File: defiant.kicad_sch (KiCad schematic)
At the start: 47 parts, among them J1 Conn_01x02_Pin, SW1 SW_Push, U1 Seeed Studio XIAO BLE

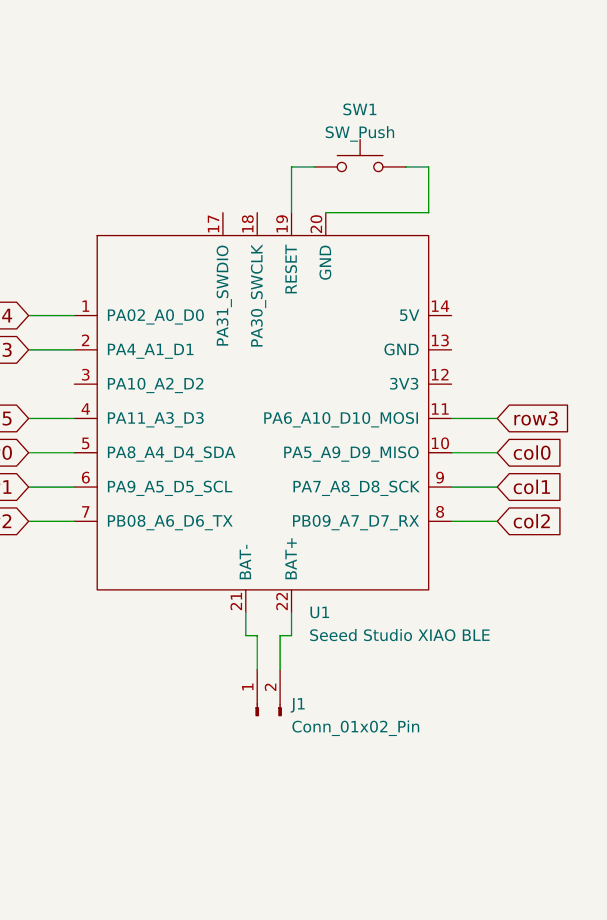
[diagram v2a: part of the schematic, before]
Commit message: Add power switch and reset button
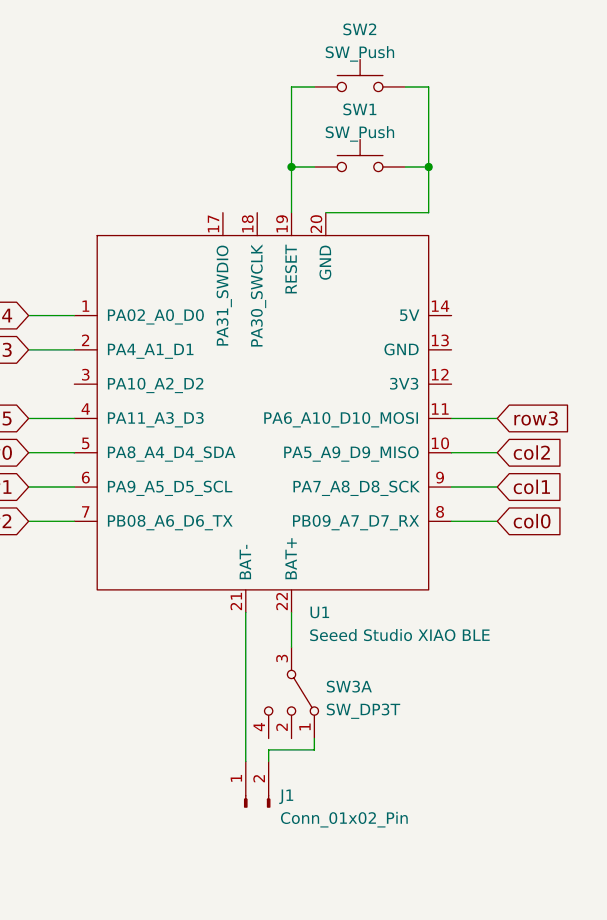
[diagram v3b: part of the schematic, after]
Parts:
- added SW2: SW_Push, Button_Switch_SMD:SW_SPST_TL3342, symbol Switch:SW_Push
- added SW3: SW_DP3T, Button_Switch_THT:SW_CuK_JS202011AQN_DPDT_Angled, symbol Switch:SW_DP3T
- SW1: footprint (none) -> Button_Switch_SMD:SW_SPST_TL3342
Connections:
- net col0: now also U1.8 (PB09_A7_D7_RX); no longer U1.10 (PA5_A9_D9_MISO)
- net col2: now also U1.10 (PA5_A9_D9_MISO); no longer U1.8 (PB09_A7_D7_RX)
- net at SW1.1, U1.19 (RESET): now also SW2.1
- net at SW1.2, U1.20 (GND): now also SW2.2
- net at U1.22 (BAT+): now also SW3.3; no longer J1.2 (Pin_2)
- new net: J1.2 (Pin_2), SW3.1
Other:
- moved on the sheet: J1
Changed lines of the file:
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@@
   (junction (at 97.79 69.85) (diameter 0) (color 0 0 0 0)
   )
+  (junction (at 243.84 27.94) (diameter 0) (color 0 0 0 0)
+  )
   (junction (at 36.83 45.72) (diameter 0) (color 0 0 0 0)
   )
@@
   (junction (at 74.93 69.85) (diameter 0) (color 0 0 0 0)
   )
+  (junction (at 228.6 27.94) (diameter 0) (color 0 0 0 0)
+  )
   (junction (at 143.51 69.85) (diameter 0) (color 0 0 0 0)
   )
@@
   (junction (at 36.83 77.47) (diameter 0) (color 0 0 0 0)
   )
-  (wire (pts (xy 224.79 83.82) (xy 224.79 80.01))
-    (stroke (width 0) (type default))
-  )
   (wire (pts (xy 105.41 62.23) (xy 105.41 77.47))
     (stroke (width 0) (type default))
@@
     (stroke (width 0) (type default))
   )
-  (wire (pts (xy 227.33 80.01) (xy 228.6 80.01))
-    (stroke (width 0) (type default))
-  )
   (wire (pts (xy 128.27 90.17) (xy 151.13 90.17))
     (stroke (width 0) (type default))
@@
     (stroke (width 0) (type default))
   )
-  (wire (pts (xy 228.6 80.01) (xy 228.6 77.47))
+  (wire (pts (xy 228.6 77.47) (xy 228.6 81.28))
     (stroke (width 0) (type default))
   )
@@
     (stroke (width 0) (type default))
   )
+  (wire (pts (xy 243.84 27.94) (xy 243.84 19.05))
+    (stroke (width 0) (type default))
+  )
   (wire (pts (xy 48.26 69.85) (xy 52.07 69.85))
     (stroke (width 0) (type default))
@@
     (stroke (width 0) (type default))
   )
+  (wire (pts (xy 231.14 19.05) (xy 228.6 19.05))
+    (stroke (width 0) (type default))
+  )
   (wire (pts (xy 74.93 53.34) (xy 97.79 53.34))
     (stroke (width 0) (type default))
@@
     (stroke (width 0) (type default))
   )
-  (wire (pts (xy 227.33 83.82) (xy 227.33 80.01))
-    (stroke (width 0) (type default))
-  )
   (wire (pts (xy 59.69 93.98) (xy 59.69 77.47))
     (stroke (width 0) (type default))
@@
     (stroke (width 0) (type default))
   )
+  (wire (pts (xy 226.06 92.71) (xy 231.14 92.71))
+    (stroke (width 0) (type default))
+  )
   (wire (pts (xy 199.39 63.5) (xy 204.47 63.5))
     (stroke (width 0) (type default))
@@
     (stroke (width 0) (type default))
   )
-  (wire (pts (xy 224.79 80.01) (xy 223.52 80.01))
-    (stroke (width 0) (type default))
-  )
   (wire (pts (xy 74.93 85.09) (xy 97.79 85.09))
     (stroke (width 0) (type default))
@@
     (stroke (width 0) (type default))
   )
+  (wire (pts (xy 243.84 19.05) (xy 241.3 19.05))
+    (stroke (width 0) (type default))
+  )
+  (wire (pts (xy 226.06 93.98) (xy 226.06 92.71))
+    (stroke (width 0) (type default))
+  )
   (wire (pts (xy 71.12 107.95) (xy 74.93 107.95))
     (stroke (width 0) (type default))
@@
     (stroke (width 0) (type default))
   )
+  (wire (pts (xy 231.14 92.71) (xy 231.14 91.44))
+    (stroke (width 0) (type default))
+  )
   (wire (pts (xy 120.65 69.85) (xy 143.51 69.85))
     (stroke (width 0) (type default))
   )
+  (wire (pts (xy 228.6 19.05) (xy 228.6 27.94))
+    (stroke (width 0) (type default))
+  )
   (wire (pts (xy 128.27 90.17) (xy 128.27 77.47))
     (stroke (width 0) (type default))
@@
     (stroke (width 0) (type default))
   )
-  (wire (pts (xy 223.52 80.01) (xy 223.52 77.47))
+  (wire (pts (xy 223.52 77.47) (xy 223.52 93.98))
     (stroke (width 0) (type default))
   )
@@
     )
   )
-  (global_label "col0" (shape input) (at 251.46 59.69 0)
+  (global_label "col2" (shape input) (at 251.46 59.69 0)
     (effects (font (size 1.524 1.524)) (justify left))
     (property "Intersheetrefs" "${INTERSHEET_REFS}" (at 251.46 59.69 0)
@@
     )
   )
-  (global_label "col2" (shape input) (at 251.46 67.31 0)
+  (global_label "col0" (shape input) (at 251.46 67.31 0)
     (effects (font (size 1.524 1.524)) (justify left))
     (property "Intersheetrefs" "${INTERSHEET_REFS}" (at 251.46 67.31 0)
@@
     )
   )
+  (symbol (lib_id "Switch:SW_Push") (at 236.22 19.05 0) (unit 1)
+    (in_bom yes) (on_board yes) (dnp no) (fields_autoplaced)
+    (property "Reference" "SW2" (at 236.22 12.7 0)
+      (effects (font (size 1.27 1.27)))
+    )
+    (property "Value" "SW_Push" (at 236.22 15.24 0)
+      (effects (font (size 1.27 1.27)))
+    )
+    (property "Footprint" "Button_Switch_SMD:SW_SPST_TL3342" (at 236.22 13.97 0)
+      (effects (font (size 1.27 1.27)) hide)
+    )
+    (property "Datasheet" "~" (at 236.22 13.97 0)
+      (effects (font (size 1.27 1.27)) hide)
+    )
+    (pin "1")
+    (pin "2")
+    (instances
+      (project "defiant"
+        (path "/cd54289a-7f2f-4953-8338-a5e4a81fda5f"
+          (reference "SW2") (unit 1)
+        )
+      )
+    )
+  )
   (symbol (lib_id "corne-chocolate-rescue:SW_PUSH-kbd") (at 156.21 62.23 0) (unit 1)
     (in_bom yes) (on_board yes) (dnp no)
@@
       (effects (font (size 1.27 1.27)))
     )
-    (property "Footprint" "" (at 236.22 22.86 0)
+    (property "Footprint" "Button_Switch_SMD:SW_SPST_TL3342" (at 236.22 22.86 0)
       (effects (font (size 1.27 1.27)) hide)
     )
@@
     )
   )
-  (symbol (lib_id "Connector:Conn_01x02_Pin") (at 224.79 88.9 90) (unit 1)
+  (symbol (lib_id "Connector:Conn_01x02_Pin") (at 223.52 99.06 90) (unit 1)
     (in_bom yes) (on_board yes) (dnp no) (fields_autoplaced)
-    (property "Reference" "J1" (at 228.6 87.63 90)
+    (property "Reference" "J1" (at 227.33 97.79 90)
       (effects (font (size 1.27 1.27)) (justify right))
     )
-    (property "Value" "Conn_01x02_Pin" (at 228.6 90.17 90)
+    (property "Value" "Conn_01x02_Pin" (at 227.33 100.33 90)
       (effects (font (size 1.27 1.27)) (justify right))
     )
-    (property "Footprint" "Seeedstudio XIAO:Lipo Connector" (at 224.79 88.9 0)
-      (effects (font (size 1.27 1.27)) hide)
-    )
-    (property "Datasheet" "~" (at 224.79 88.9 0)
+    (property "Footprint" "Seeedstudio XIAO:Lipo Connector" (at 223.52 99.06 0)
+      (effects (font (size 1.27 1.27)) hide)
+    )
+    (property "Datasheet" "~" (at 223.52 99.06 0)
       (effects (font (size 1.27 1.27)) hide)
     )
@@
         )
       )
+    )
+  )
+  (symbol (lib_id "Switch:SW_DP3T") (at 228.6 86.36 270) (unit 1)
+    (in_bom yes) (on_board yes) (dnp no) (fields_autoplaced)
+    (property "Reference" "SW3" (at 232.41 85.725 90)
+      (effects (font (size 1.27 1.27)) (justify left))
+    )
+    (property "Value" "SW_DP3T" (at 232.41 88.265 90)
+      (effects (font (size 1.27 1.27)) (justify left))
+    )
+    (property "Footprint" "Button_Switch_THT:SW_CuK_JS202011AQN_DPDT_Angled" (at 233.045 70.485 0)
+      (effects (font (size 1.27 1.27)) hide)
+    )
+    (property "Datasheet" "~" (at 233.045 70.485 0)
+      (effects (font (size 1.27 1.27)) hide)
+    )
+    (pin "1")
+    (pin "2")
+    (pin "3")
+    (pin "4")
+    (pin "5")
+    (pin "6")
+    (pin "7")
+    (pin "8")
+    (instances
+      (project "defiant"
+        (path "/cd54289a-7f2f-4953-8338-a5e4a81fda5f"
+          (reference "SW3") (unit 1)
+        )
+      )

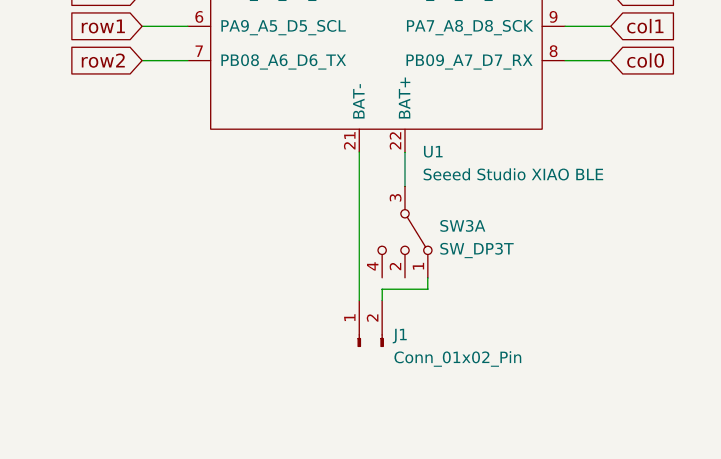
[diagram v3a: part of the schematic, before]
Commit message: Fix power switch wiring
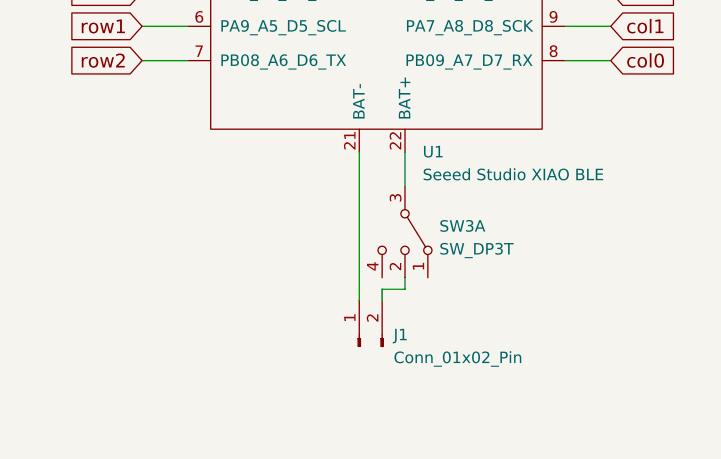
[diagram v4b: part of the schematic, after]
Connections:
- net at J1.2 (Pin_2): now also SW3.2; no longer SW3.1
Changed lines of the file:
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@@
+    (stroke (width 0) (type default))
+  )
+  (wire (pts (xy 226.06 92.71) (xy 228.6 92.71))
     (stroke (width 0) (type default))
   )
@@
     (stroke (width 0) (type default))
   )
-  (wire (pts (xy 59.69 62.23) (xy 59.69 77.47))
+  (wire (pts (xy 228.6 92.71) (xy 228.6 91.44))
     (stroke (width 0) (type default))
   )
-  (wire (pts (xy 226.06 92.71) (xy 231.14 92.71))
+  (wire (pts (xy 59.69 62.23) (xy 59.69 77.47))
     (stroke (width 0) (type default))
   )
@@
     (stroke (width 0) (type default))
   )
-  (wire (pts (xy 231.14 92.71) (xy 231.14 91.44))
-    (stroke (width 0) (type default))
-  )
